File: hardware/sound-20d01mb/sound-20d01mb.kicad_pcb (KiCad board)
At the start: 2 copper layers, 0 parts

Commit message: Updated PCB
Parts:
- added C1: 0.1uF, Capacitor_SMD:C_1206_3216Metric_Pad1.42x1.75mm_HandSolder, F.Cu at (123.2, 76.2)
- added C10: 0.1uF, Capacitor_SMD:C_1206_3216Metric_Pad1.42x1.75mm_HandSolder, F.Cu at (106.7, 48.3)
- added C11: 1uF, Capacitor_SMD:C_1206_3216Metric_Pad1.42x1.75mm_HandSolder, F.Cu at (138.4, 58.4)
- added C12: 0.1uF, Capacitor_SMD:C_1206_3216Metric_Pad1.42x1.75mm_HandSolder, F.Cu at (138.4, 62.2)
- added C13: 0.1uF, Capacitor_SMD:C_1206_3216Metric_Pad1.42x1.75mm_HandSolder, F.Cu at (133.3, 54.6)
- added C14: 0.1uF, Capacitor_SMD:C_1206_3216Metric_Pad1.42x1.75mm_HandSolder, F.Cu at (121.3, 54.0)
- added C15: 4.7uF, Capacitor_SMD:C_1206_3216Metric_Pad1.42x1.75mm_HandSolder, F.Cu at (125.7, 52.1)
- added C16: 0.1uF, Capacitor_SMD:C_1206_3216Metric_Pad1.42x1.75mm_HandSolder, F.Cu at (197.5, 62.2)
- added C17: 10uF, Capacitor_SMD:CP_Elec_4x5.4, F.Cu at (197.5, 52.1)
- added C18: 2.2nF, Capacitor_THT:C_Rect_L7.2mm_W2.5mm_P5.00mm_FKS2_FKP2_MKS2_MKP2, F.Cu at (205.3, 59.1)
- added C19: 2.2uF, Capacitor_SMD:C_1206_3216Metric_Pad1.42x1.75mm_HandSolder, F.Cu at (190.5, 73.0)
- added C2: 0.1uF, Capacitor_SMD:C_1206_3216Metric_Pad1.42x1.75mm_HandSolder, F.Cu at (132.7, 73.0)
- added C20: 2.2uF, Capacitor_SMD:C_1206_3216Metric_Pad1.42x1.75mm_HandSolder, F.Cu at (197.5, 68.6)
- added C21: 10uF, Capacitor_SMD:CP_Elec_4x5.4, F.Cu at (177.8, 67.3)
- added C22: 0.1uF, Capacitor_SMD:C_1206_3216Metric_Pad1.42x1.75mm_HandSolder, F.Cu at (183.5, 67.3)
- added C23: 2.2nF, Capacitor_THT:C_Rect_L7.2mm_W2.5mm_P5.00mm_FKS2_FKP2_MKS2_MKP2, F.Cu at (205.3, 71.8)
- added C24: 10uF, Capacitor_SMD:CP_Elec_4x5.4, F.Cu at (183.5, 78.7)
- added C25: 0.1uF, Capacitor_SMD:C_1206_3216Metric_Pad1.42x1.75mm_HandSolder, F.Cu at (183.5, 73.0)
- added C26: 0.1uF, Capacitor_SMD:C_1206_3216Metric_Pad1.42x1.75mm_HandSolder, F.Cu at (197.5, 73.0)
- added C27: 10uF, Capacitor_SMD:CP_Elec_4x5.4, F.Cu at (197.5, 78.7)
- added C28: 0.1uF, Capacitor_SMD:C_1206_3216Metric_Pad1.42x1.75mm_HandSolder, F.Cu at (229.9, 57.1)
- added C29: 470uF, Capacitor_THT:CP_Radial_D12.5mm_P5.00mm, F.Cu at (226.1, 44.5)
- added C3: 0.1uF, Capacitor_SMD:C_1206_3216Metric_Pad1.42x1.75mm_HandSolder, F.Cu at (117.5, 69.2)
- added C30: 0.1uF, Capacitor_SMD:C_1206_3216Metric_Pad1.42x1.75mm_HandSolder, F.Cu at (236.2, 55.9)
- added C31: 10uF, Capacitor_SMD:C_1210_3225Metric_Pad1.42x2.65mm_HandSolder, F.Cu at (241.3, 38.1)
- added C32: 4700uF, Capacitor_THT:CP_Radial_D18.0mm_P7.50mm, F.Cu at (269.2, 55.9)
- added C33: 2.2uF, Capacitor_SMD:C_1206_3216Metric_Pad1.42x1.75mm_HandSolder, F.Cu at (215.9, 67.3)
- added C34: 0.68uF, Capacitor_THT:C_Rect_L7.2mm_W4.5mm_P5.00mm_FKS2_FKP2_MKS2_MKP2, F.Cu at (256.5, 77.5)
- added C35: 0.22uF, Capacitor_SMD:C_1206_3216Metric_Pad1.42x1.75mm_HandSolder, F.Cu at (238.8, 61.0)
- added C36: 0.22uF, Capacitor_SMD:C_1206_3216Metric_Pad1.42x1.75mm_HandSolder, F.Cu at (238.5, 66.0)
- added C37: 2.2uF, Capacitor_SMD:C_1206_3216Metric_Pad1.42x1.75mm_HandSolder, F.Cu at (215.9, 63.5)
- added C38: 0.68uF, Capacitor_THT:C_Rect_L7.2mm_W4.5mm_P5.00mm_FKS2_FKP2_MKS2_MKP2, F.Cu at (256.5, 55.9)
- added C39: 4700uF, Capacitor_THT:CP_Radial_D18.0mm_P7.50mm, F.Cu at (269.2, 77.5)
- added C4: 0.1uF, Capacitor_SMD:C_1206_3216Metric_Pad1.42x1.75mm_HandSolder, F.Cu at (76.2, 53.3)
- added C40: 2.2uF, Capacitor_SMD:C_1206_3216Metric_Pad1.42x1.75mm_HandSolder, F.Cu at (222.2, 62.2)
- added C41: 1uF, Capacitor_SMD:C_1206_3216Metric_Pad1.42x1.75mm_HandSolder, F.Cu at (222.2, 67.3)
- added C42: 0.1uF, Capacitor_SMD:C_1206_3216Metric_Pad1.42x1.75mm_HandSolder, F.Cu at (229.9, 72.4)
- added C43: 470uF, Capacitor_THT:CP_Radial_D12.5mm_P5.00mm, F.Cu at (226.1, 83.8)
- added C44: 47uF, Capacitor_SMD:CP_Elec_6.3x5.4, F.Cu at (76.2, 71.1)
- added C45: 10uF, Capacitor_SMD:CP_Elec_4x5.4, F.Cu at (49.5, 71.1)
- added C46: 2.2uF, Capacitor_SMD:C_1206_3216Metric_Pad1.42x1.75mm_HandSolder, F.Cu at (49.5, 77.5)
- added C47: 2.2uF, Capacitor_SMD:C_1206_3216Metric_Pad1.42x1.75mm_HandSolder, F.Cu at (67.3, 73.7)
- added C48: 10uF, Capacitor_SMD:CP_Elec_4x5.4, F.Cu at (67.3, 80.0)
- added C49: 10uF, Capacitor_SMD:CP_Elec_4x5.4, F.Cu at (176.5, 132.1)
- added C5: 0.1uF, Capacitor_SMD:C_1206_3216Metric_Pad1.42x1.75mm_HandSolder, F.Cu at (144.8, 62.2)
- added C50: 2.2uF, Capacitor_SMD:C_1206_3216Metric_Pad1.42x1.75mm_HandSolder, F.Cu at (146.1, 121.9)
- added C51: 2.2uF, Capacitor_SMD:C_1206_3216Metric_Pad1.42x1.75mm_HandSolder, F.Cu at (177.8, 113.0)
- added C52: 47uF, Capacitor_SMD:CP_Elec_6.3x5.4, F.Cu at (196.8, 132.1)
- added C53: 0.33uF, Capacitor_SMD:C_1206_3216Metric_Pad1.42x1.75mm_HandSolder, F.Cu at (189.2, 115.6)
- added C54: 0.1uF, Capacitor_SMD:C_1206_3216Metric_Pad1.42x1.75mm_HandSolder, F.Cu at (189.2, 121.9)
- added C55: 10uF, Capacitor_SMD:CP_Elec_4x5.4, F.Cu at (185.4, 132.1)
- added C6: 15pF, Capacitor_SMD:C_1206_3216Metric_Pad1.42x1.75mm_HandSolder, F.Cu at (142.2, 81.3)
- added C7: 15pF, Capacitor_SMD:C_1206_3216Metric_Pad1.42x1.75mm_HandSolder, F.Cu at (135.9, 81.3)
- added C8: 22pF, Capacitor_SMD:C_1206_3216Metric_Pad1.42x1.75mm_HandSolder, F.Cu at (149.2, 74.9)
- added C9: 22pF, Capacitor_SMD:C_1206_3216Metric_Pad1.42x1.75mm_HandSolder, F.Cu at (149.2, 67.3)
- added D1: AMP_LED, LED_SMD:LED_1206_3216Metric_Pad1.42x1.75mm_HandSolder, F.Cu at (152.4, 106.7)
- added D2: MUTE_LED, LED_SMD:LED_1206_3216Metric_Pad1.42x1.75mm_HandSolder, F.Cu at (152.4, 111.8)
- added D3: CRS04, Diode_SMD:D_SOD-123F, F.Cu at (76.2, 63.5)
- added D4: D_PWR_LED, LED_SMD:LED_1206_3216Metric_Pad1.42x1.75mm_HandSolder, F.Cu at (73.7, 86.4)
- added D5: A_PWR_LED, LED_SMD:LED_1206_3216Metric_Pad1.42x1.75mm_HandSolder, F.Cu at (152.4, 121.9)
- added F1: MF-MSMF050-2, Fuse:Fuse_1812_4532Metric_Pad1.30x3.40mm_HandSolder, F.Cu at (76.2, 58.4)
- added H1: MountingHole_Pad, MountingHole:MountingHole_3.2mm_M3_Pad_Via, F.Cu at (38.1, 27.9)
- added H2: MountingHole_Pad, MountingHole:MountingHole_3.2mm_M3_Pad_Via, F.Cu at (270.5, 25.4)
- added H3: MountingHole_Pad, MountingHole:MountingHole_3.2mm_M3_Pad_Via, F.Cu at (35.6, 118.1)
- added H4: MountingHole_Pad, MountingHole:MountingHole_3.2mm_M3_Pad_Via, F.Cu at (271.8, 125.7)
- added J1: USB_B, Connector_USB:USB_B_OST_USB-B1HSxx_Horizontal, F.Cu at (68.6, 58.4)
- added J10: Conn_01x02, Connector_JST:JST_VH_B2P-VH_1x02_P3.96mm_Vertical, F.Cu at (224.8, 104.1)
- added J11: Conn_01x03, Connector_PinHeader_2.54mm:PinHeader_1x03_P2.54mm_Vertical, F.Cu at (166.4, 39.4)
- added J12: Conn_01x04, Connector_PinHeader_2.54mm:PinHeader_1x04_P2.54mm_Vertical, F.Cu at (189.2, 47.0)
- added J13: Conn_01x06, Connector_PinHeader_2.54mm:PinHeader_1x06_P2.54mm_Vertical, F.Cu at (151.1, 39.4)
- added J14: Conn_01x03, Connector_PinHeader_2.54mm:PinHeader_1x03_P2.54mm_Vertical, F.Cu at (208.3, 67.9)
- added J2: Conn_01x04, sound-20d01mb:X977B04, F.Cu at (250.2, 105.4)
- added J3: Conn_02x08_Odd_Even, Connector_PinHeader_2.54mm:PinHeader_2x08_P2.54mm_Vertical, F.Cu at (94.0, 72.4)
- added J4: Conn_02x04_Odd_Even, Connector_PinHeader_2.54mm:PinHeader_2x04_P2.54mm_Vertical, F.Cu at (212.1, 100.3)
- added J5: Conn_01x06, Connector_PinHeader_2.54mm:PinHeader_1x06_P2.54mm_Vertical, F.Cu at (109.2, 68.6)
- added J6: Conn_02x10_Odd_Even, Connector_PinHeader_2.54mm:PinHeader_2x10_P2.54mm_Vertical, F.Cu at (138.4, 41.9)
- added J7: Conn_02x10_Odd_Even, Connector_PinHeader_2.54mm:PinHeader_2x10_P2.54mm_Vertical, F.Cu at (138.4, 87.6)
- added J8: Conn_01x02, Connector_JST:JST_XH_B02B-XH-A_1x02_P2.50mm_Vertical, F.Cu at (49.5, 94.0)
- added J9: Conn_01x02, Connector_JST:JST_XH_B02B-XH-A_1x02_P2.50mm_Vertical, F.Cu at (61.0, 94.0)
- added JP1: Jumper_NC_Dual, Connector_PinHeader_2.54mm:PinHeader_1x03_P2.54mm_Vertical, F.Cu at (96.5, 58.4)
- added JP2: Jumper_3_Bridged12, Connector_PinHeader_2.54mm:PinHeader_1x03_P2.54mm_Vertical, F.Cu at (128.3, 76.2)
- added L1: 22uH, Inductor_SMD:L_Bourns_SRR1260, F.Cu at (246.4, 50.8)
- added L2: 22uH, Inductor_SMD:L_Bourns_SRR1260, F.Cu at (246.4, 77.5)
- added NT1: Net-Tie_2, NetTie:NetTie-2_SMD_Pad2.0mm, F.Cu at (190.5, 76.2)
- added R1: 10K, Resistor_SMD:R_1206_3216Metric_Pad1.42x1.75mm_HandSolder, F.Cu at (104.1, 73.7)
- added R10: 10K, Resistor_SMD:R_1206_3216Metric_Pad1.42x1.75mm_HandSolder, F.Cu at (197.5, 57.8)
- added R11: 22R, Resistor_SMD:R_1206_3216Metric_Pad1.42x1.75mm_HandSolder, F.Cu at (180.3, 53.3)
- added R12: 22R, Resistor_SMD:R_1206_3216Metric_Pad1.42x1.75mm_HandSolder, F.Cu at (180.3, 57.1)
- added R13: 470R, Resistor_SMD:R_1206_3216Metric_Pad1.42x1.75mm_HandSolder, F.Cu at (203.8, 67.3)
- added R14: 22R, Resistor_SMD:R_1206_3216Metric_Pad1.42x1.75mm_HandSolder, F.Cu at (180.3, 61.0)
- added R15: 4.7K, Resistor_SMD:R_1206_3216Metric_Pad1.42x1.75mm_HandSolder, F.Cu at (260.4, 62.2)
- added R16: 4.7K, Resistor_SMD:R_1206_3216Metric_Pad1.42x1.75mm_HandSolder, F.Cu at (260.4, 69.8)
- added R17: 10K, Resistor_SMD:R_1206_3216Metric_Pad1.42x1.75mm_HandSolder, F.Cu at (237.5, 91.4)
- added R18: 10K, Resistor_SMD:R_1206_3216Metric_Pad1.42x1.75mm_HandSolder, F.Cu at (237.5, 96.5)
- added R19: 1K, Resistor_SMD:R_1206_3216Metric_Pad1.42x1.75mm_HandSolder, F.Cu at (181.6, 94.0)
- added R2: 4.7K, Resistor_SMD:R_1206_3216Metric_Pad1.42x1.75mm_HandSolder, F.Cu at (160.0, 39.4)
- added R20: 1K, Resistor_SMD:R_1206_3216Metric_Pad1.42x1.75mm_HandSolder, F.Cu at (181.6, 102.9)
- added R21: 1K, Resistor_SMD:R_1206_3216Metric_Pad1.42x1.75mm_HandSolder, F.Cu at (158.8, 106.7)
- added R22: 10K, Resistor_SMD:R_1206_3216Metric_Pad1.42x1.75mm_HandSolder, F.Cu at (215.9, 55.9)
- added R23: 1K, Resistor_SMD:R_1206_3216Metric_Pad1.42x1.75mm_HandSolder, F.Cu at (158.8, 111.8)
- added R24: 10K, Resistor_SMD:R_1206_3216Metric_Pad1.42x1.75mm_HandSolder, F.Cu at (222.2, 55.9)
- added R25: 330R, Resistor_SMD:R_1206_3216Metric_Pad1.42x1.75mm_HandSolder, F.Cu at (67.3, 86.4)
- added R26: 1K, Resistor_SMD:R_1206_3216Metric_Pad1.42x1.75mm_HandSolder, F.Cu at (158.8, 121.9)
- added R3: 4.7K, Resistor_SMD:R_1206_3216Metric_Pad1.42x1.75mm_HandSolder, F.Cu at (160.0, 44.5)
- added R4: 22R, Resistor_SMD:R_1206_3216Metric_Pad1.42x1.75mm_HandSolder, F.Cu at (82.5, 46.4)
- added R5: 22R, Resistor_SMD:R_1206_3216Metric_Pad1.42x1.75mm_HandSolder, F.Cu at (82.5, 50.2)
- added R6: 390R, Resistor_SMD:R_1206_3216Metric_Pad1.42x1.75mm_HandSolder, F.Cu at (138.4, 66.0)
- added R7: 51R, Resistor_SMD:R_1206_3216Metric_Pad1.42x1.75mm_HandSolder, F.Cu at (114.3, 53.3)
- added R8: 22R, Resistor_SMD:R_1206_3216Metric_Pad1.42x1.75mm_HandSolder, F.Cu at (180.3, 49.5)
- added R9: 470R, Resistor_SMD:R_1206_3216Metric_Pad1.42x1.75mm_HandSolder, F.Cu at (203.8, 63.5)
- added SW1: SW_DIP_x02, Button_Switch_THT:SW_DIP_SPSTx02_Slide_9.78x7.26mm_W7.62mm_P2.54mm, F.Cu at (242.6, 88.9)
- added U1: USBLC6-2SC6, Package_TO_SOT_SMD:SOT-23-6, F.Cu at (76.2, 48.3)
- added U2: STM32F446RCTx, Package_QFP:LQFP-64_10x10mm_P0.5mm, F.Cu at (127.0, 63.5)
- added U3: PCM5142, Package_SO:TSSOP-28_4.4x9.7mm_P0.65mm, F.Cu at (190.5, 64.8)
- added U4: TPA3123D2, Package_SO:HTSSOP-24-1EP_4.4x7.8mm_P0.65mm_EP3.4x7.8mm_Mask2.4x4.68mm_ThermalVias, F.Cu at (229.9, 64.8)
- added U5: PC817, Package_DIP:DIP-4_W7.62mm, F.Cu at (186.7, 94.0)
- added U6: PC817, Package_DIP:DIP-4_W7.62mm, F.Cu at (186.7, 102.9)
- added U7: ADP3338AKCZ-3.3RL7, Package_TO_SOT_SMD:SOT-223-3_TabPin2, F.Cu at (59.7, 73.7)
- added U8: ADP3338AKCZ-3.3RL7, Package_TO_SOT_SMD:SOT-223-3_TabPin2, F.Cu at (180.3, 120.7)
- added U9: L7805ABD2T-TR, Package_TO_SOT_SMD:TO-263-2, F.Cu at (200.7, 119.4)
- added X1: SM7745HEV-12.288M, Oscillator:Oscillator_SMD_Fordahl_DFAS2-4Pin_7.3x5.1mm_HandSoldering, F.Cu at (106.7, 55.9)
- added Y1: 32.768kHz, Crystal:Crystal_SMD_3215-2Pin_3.2x1.5mm, F.Cu at (138.4, 76.2)
- added Y2: 8MHz, Crystal:Crystal_SMD_HC49-SD, F.Cu at (144.8, 71.1)
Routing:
- net +3V3: track 0.00 -> 66.7 mm, vias 0 -> 7
- net +3.3VA: track 0.00 -> 42.6 mm, vias 0 -> 2
- net /Microcontroller Unit/RCC_OSC_IN: track 0.00 -> 23.3 mm
- net DAC_GPIO6: track 0.00 -> 19.2 mm, vias 0 -> 1
- net Net-(R8-Pad2): track 0.00 -> 18.1 mm
- net I2C1_SDA: track 0.00 -> 17.5 mm
- net I2C1_SCL: track 0.00 -> 17.4 mm
- net VBUS: track 0.00 -> 17.4 mm
- net /Microcontroller Unit/USB_D+: track 0.00 -> 16.0 mm
- net DAC_GPIO3: track 0.00 -> 15.9 mm, vias 0 -> 1
- net Net-(R11-Pad2): track 0.00 -> 15.3 mm
- net /Microcontroller Unit/USB_D-: track 0.00 -> 13.1 mm
- net /Microcontroller Unit/NRST: track 0.00 -> 12.3 mm
- net Net-(R12-Pad2): track 0.00 -> 11.8 mm
- net Net-(C21-Pad1): track 0.00 -> 10.8 mm
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- added copper zone on B.Cu, net GNDA
- added copper zone on F.Cu, net GNDA
- added copper zone on B.Cu, net GNDD
- added copper zone on F.Cu, net GNDD
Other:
- board text added: "3"
- board text added: "4"
- board text added: "5"
- board text added: "6"

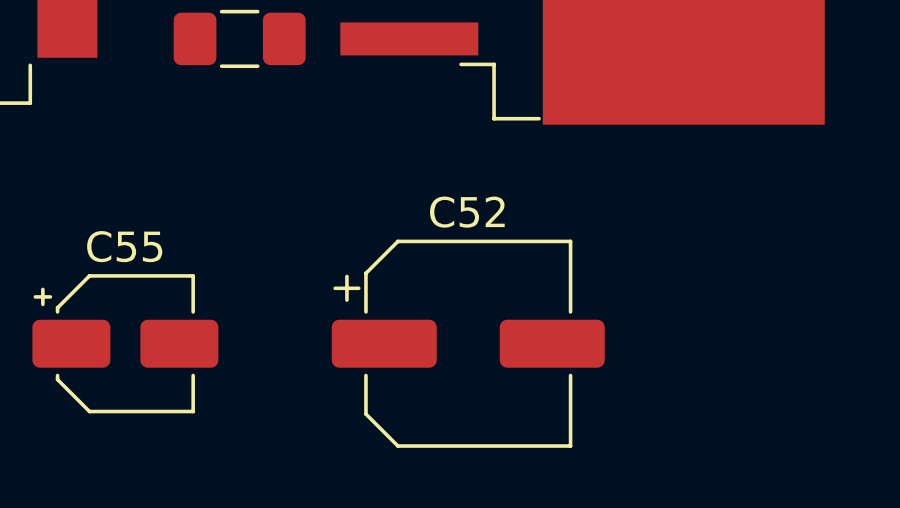
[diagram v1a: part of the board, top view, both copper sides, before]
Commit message: Updated C52 footprint
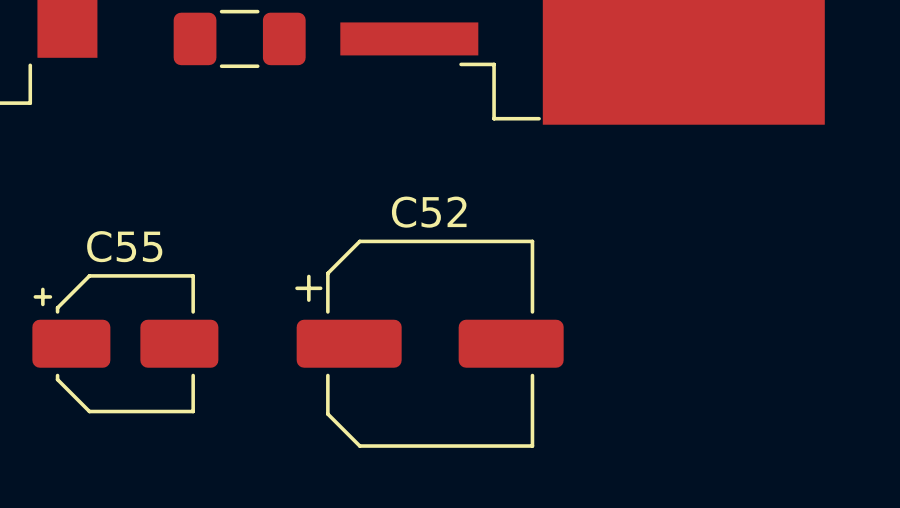
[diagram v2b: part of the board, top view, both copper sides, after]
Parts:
- C52: footprint Capacitor_SMD:CP_Elec_6.3x5.4 -> Capacitor_SMD:CP_Elec_6.3x7.7
- moved C52 1.27 mm to (195.6, 132.1)
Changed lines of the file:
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@@
     )
   )
-  (module Capacitor_SMD:CP_Elec_6.3x5.4 (layer F.Cu)
-    (at 196.85 132.08)
-    (descr "SMD capacitor, aluminum electrolytic, Panasonic C55, 6.3x5.4mm")
-    (tags "capacitor electrolytic")
-    (attr smd)
-    (fp_text reference C52 (at 0 -4.35) (layer F.SilkS)
-      (effects (font (size 1 1) (thickness 0.15)))
-    )
-    (fp_text value 47uF (at 0 4.35) (layer F.Fab)
-      (effects (font (size 1 1) (thickness 0.15)))
-    )
-    (fp_circle (center 0 0) (end 3.15 0) (layer F.Fab) (width 0.1))
-    (fp_line (start 3.3 -3.3) (end 3.3 3.3) (layer F.Fab) (width 0.1))
-    (fp_line (start -2.3 -3.3) (end 3.3 -3.3) (layer F.Fab) (width 0.1))
-    (fp_line (start -2.3 3.3) (end 3.3 3.3) (layer F.Fab) (width 0.1))
-    (fp_line (start -3.3 -2.3) (end -3.3 2.3) (layer F.Fab) (width 0.1))
-    (fp_line (start -3.3 -2.3) (end -2.3 -3.3) (layer F.Fab) (width 0.1))
-    (fp_line (start -3.3 2.3) (end -2.3 3.3) (layer F.Fab) (width 0.1))
-    (fp_line (start -2.704838 -1.33) (end -2.074838 -1.33) (layer F.Fab) (width 0.1))
-    (fp_line (start -2.389838 -1.645) (end -2.389838 -1.015) (layer F.Fab) (width 0.1))
-    (fp_line (start 3.41 3.41) (end 3.41 1.06) (layer F.SilkS) (width 0.12))
-    (fp_line (start 3.41 -3.41) (end 3.41 -1.06) (layer F.SilkS) (width 0.12))
-    (fp_line (start -2.345563 -3.41) (end 3.41 -3.41) (layer F.SilkS) (width 0.12))
-    (fp_line (start -2.345563 3.41) (end 3.41 3.41) (layer F.SilkS) (width 0.12))
-    (fp_line (start -3.41 2.345563) (end -3.41 1.06) (layer F.SilkS) (width 0.12))
-    (fp_line (start -3.41 -2.345563) (end -3.41 -1.06) (layer F.SilkS) (width 0.12))
-    (fp_line (start -3.41 -2.345563) (end -2.345563 -3.41) (layer F.SilkS) (width 0.12))
-    (fp_line (start -3.41 2.345563) (end -2.345563 3.41) (layer F.SilkS) (width 0.12))
-    (fp_line (start -4.4375 -1.8475) (end -3.65 -1.8475) (layer F.SilkS) (width 0.12))
-    (fp_line (start -4.04375 -2.24125) (end -4.04375 -1.45375) (layer F.SilkS) (width 0.12))
-    (fp_line (start 3.55 -3.55) (end 3.55 -1.05) (layer F.CrtYd) (width 0.05))
-    (fp_line (start 3.55 -1.05) (end 4.8 -1.05) (layer F.CrtYd) (width 0.05))
-    (fp_line (start 4.8 -1.05) (end 4.8 1.05) (layer F.CrtYd) (width 0.05))
-    (fp_line (start 4.8 1.05) (end 3.55 1.05) (layer F.CrtYd) (width 0.05))
-    (fp_line (start 3.55 1.05) (end 3.55 3.55) (layer F.CrtYd) (width 0.05))
-    (fp_line (start -2.4 3.55) (end 3.55 3.55) (layer F.CrtYd) (width 0.05))
-    (fp_line (start -2.4 -3.55) (end 3.55 -3.55) (layer F.CrtYd) (width 0.05))
-    (fp_line (start -3.55 2.4) (end -2.4 3.55) (layer F.CrtYd) (width 0.05))
-    (fp_line (start -3.55 -2.4) (end -2.4 -3.55) (layer F.CrtYd) (width 0.05))
-    (fp_line (start -3.55 -2.4) (end -3.55 -1.05) (layer F.CrtYd) (width 0.05))
-    (fp_line (start -3.55 1.05) (end -3.55 2.4) (layer F.CrtYd) (width 0.05))
-    (fp_line (start -3.55 -1.05) (end -4.8 -1.05) (layer F.CrtYd) (width 0.05))
-    (fp_line (start -4.8 -1.05) (end -4.8 1.05) (layer F.CrtYd) (width 0.05))
-    (fp_line (start -4.8 1.05) (end -3.55 1.05) (layer F.CrtYd) (width 0.05))
-    (fp_text user %R (at 0 0) (layer F.Fab)
-      (effects (font (size 1 1) (thickness 0.15)))
-    )
-    (pad 1 smd roundrect (at -2.8 0) (size 3.5 1.6) (layers F.Cu F.Paste F.Mask) (roundrect_rratio 0.15625)
-      (net 18 VCC))
-    (pad 2 smd roundrect (at 2.8 0) (size 3.5 1.6) (layers F.Cu F.Paste F.Mask) (roundrect_rratio 0.15625)
-      (net 11 GNDA))
-    (model ${KISYS3DMOD}/Capacitor_SMD.3dshapes/CP_Elec_6.3x5.4.wrl
-      (at (xyz 0 0 0))
-      (scale (xyz 1 1 1))
-      (rotate (xyz 0 0 0))
-    )
-  )
   (module Capacitor_SMD:C_1206_3216Metric_Pad1.42x1.75mm_HandSolder (layer F.Cu)
     (at 189.23 115.57)
@@
       (at (xyz 0 0 0))
       (scale (xyz 1 1 1))
+      (rotate (xyz 0 0 0))
+    )
+  )
+  (module Capacitor_SMD:CP_Elec_6.3x7.7 (layer F.Cu)
+    (at 195.58 132.08)
+    (descr "SMD capacitor, aluminum electrolytic, Nichicon, 6.3x7.7mm")
+    (tags "capacitor electrolytic")
+    (attr smd)
+    (fp_text reference C52 (at 0 -4.35) (layer F.SilkS)
+      (effects (font (size 1 1) (thickness 0.15)))
+    )
+    (fp_text value 47uF (at 0 4.35) (layer F.Fab)
+      (effects (font (size 1 1) (thickness 0.15)))
+    )
+    (fp_circle (center 0 0) (end 3.15 0) (layer F.Fab) (width 0.1))
+    (fp_line (start 3.3 -3.3) (end 3.3 3.3) (layer F.Fab) (width 0.1))
+    (fp_line (start -2.3 -3.3) (end 3.3 -3.3) (layer F.Fab) (width 0.1))
+    (fp_line (start -2.3 3.3) (end 3.3 3.3) (layer F.Fab) (width 0.1))
+    (fp_line (start -3.3 -2.3) (end -3.3 2.3) (layer F.Fab) (width 0.1))
+    (fp_line (start -3.3 -2.3) (end -2.3 -3.3) (layer F.Fab) (width 0.1))
+    (fp_line (start -3.3 2.3) (end -2.3 3.3) (layer F.Fab) (width 0.1))
+    (fp_line (start -2.704838 -1.33) (end -2.074838 -1.33) (layer F.Fab) (width 0.1))
+    (fp_line (start -2.389838 -1.645) (end -2.389838 -1.015) (layer F.Fab) (width 0.1))
+    (fp_line (start 3.41 3.41) (end 3.41 1.06) (layer F.SilkS) (width 0.12))
+    (fp_line (start 3.41 -3.41) (end 3.41 -1.06) (layer F.SilkS) (width 0.12))
+    (fp_line (start -2.345563 -3.41) (end 3.41 -3.41) (layer F.SilkS) (width 0.12))
+    (fp_line (start -2.345563 3.41) (end 3.41 3.41) (layer F.SilkS) (width 0.12))
+    (fp_line (start -3.41 2.345563) (end -3.41 1.06) (layer F.SilkS) (width 0.12))
+    (fp_line (start -3.41 -2.345563) (end -3.41 -1.06) (layer F.SilkS) (width 0.12))
+    (fp_line (start -3.41 -2.345563) (end -2.345563 -3.41) (layer F.SilkS) (width 0.12))
+    (fp_line (start -3.41 2.345563) (end -2.345563 3.41) (layer F.SilkS) (width 0.12))
+    (fp_line (start -4.4375 -1.8475) (end -3.65 -1.8475) (layer F.SilkS) (width 0.12))
+    (fp_line (start -4.04375 -2.24125) (end -4.04375 -1.45375) (layer F.SilkS) (width 0.12))
+    (fp_line (start 3.55 -3.55) (end 3.55 -1.05) (layer F.CrtYd) (width 0.05))
+    (fp_line (start 3.55 -1.05) (end 4.7 -1.05) (layer F.CrtYd) (width 0.05))
+    (fp_line (start 4.7 -1.05) (end 4.7 1.05) (layer F.CrtYd) (width 0.05))
+    (fp_line (start 4.7 1.05) (end 3.55 1.05) (layer F.CrtYd) (width 0.05))
+    (fp_line (start 3.55 1.05) (end 3.55 3.55) (layer F.CrtYd) (width 0.05))
+    (fp_line (start -2.4 3.55) (end 3.55 3.55) (layer F.CrtYd) (width 0.05))
+    (fp_line (start -2.4 -3.55) (end 3.55 -3.55) (layer F.CrtYd) (width 0.05))
+    (fp_line (start -3.55 2.4) (end -2.4 3.55) (layer F.CrtYd) (width 0.05))
+    (fp_line (start -3.55 -2.4) (end -2.4 -3.55) (layer F.CrtYd) (width 0.05))
+    (fp_line (start -3.55 -2.4) (end -3.55 -1.05) (layer F.CrtYd) (width 0.05))
+    (fp_line (start -3.55 1.05) (end -3.55 2.4) (layer F.CrtYd) (width 0.05))
+    (fp_line (start -3.55 -1.05) (end -4.7 -1.05) (layer F.CrtYd) (width 0.05))
+    (fp_line (start -4.7 -1.05) (end -4.7 1.05) (layer F.CrtYd) (width 0.05))
+    (fp_line (start -4.7 1.05) (end -3.55 1.05) (layer F.CrtYd) (width 0.05))
+    (fp_text user %R (at 0 0) (layer F.Fab)
+      (effects (font (size 1 1) (thickness 0.15)))
+    )
+    (pad 1 smd roundrect (at -2.7 0) (size 3.5 1.6) (layers F.Cu F.Paste F.Mask) (roundrect_rratio 0.15625)
+      (net 18 VCC))
+    (pad 2 smd roundrect (at 2.7 0) (size 3.5 1.6) (layers F.Cu F.Paste F.Mask) (roundrect_rratio 0.15625)
+      (net 11 GNDA))
+    (model ${KISYS3DMOD}/Capacitor_SMD.3dshapes/CP_Elec_6.3x7.7.wrl
+      (at (xyz 0 0 0))
+      (scale (xyz 1 1 1))

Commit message: Updated PCB
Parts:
- moved H4 84.0 mm to (193.0, 96.5)
- moved H2 78.0 mm to (193.0, 34.3)
- moved D1 73.8 mm to (186.7, 41.3), turned to 180 degrees
- moved D2 71.6 mm to (186.7, 48.9), turned to 180 degrees
- moved R21 69.1 mm to (181.0, 41.3)
- moved R23 66.7 mm to (181.0, 48.9)
- moved J8 60.8 mm to (76.2, 39.4)
- moved J9 60.2 mm to (86.4, 39.4)
- moved U6 59.2 mm to (168.9, 46.4)
- moved R20 59.1 mm to (164.5, 46.4)
- moved U5 58.0 mm to (168.9, 38.7)
- moved R19 57.8 mm to (164.5, 38.7)
- moved J3 44.0 mm to (125.7, 102.9)
- moved H3 39.5 mm to (68.6, 96.5)
- moved C5 34.7 mm to (114.3, 78.7)
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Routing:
- net +3.3VA: track 42.6 -> 73.0 mm
- net /Microcontroller Unit/RCC_OSC32_OUT: track 0.00 -> 12.9 mm
- net /Microcontroller Unit/NRST: track 12.3 -> 0.00 mm
- net /Microcontroller Unit/RCC_OSC32_IN: track 0.00 -> 10.2 mm
- net /DAC/DAC_WS: track 0.00 -> 4.64 mm
- net /Microcontroller Unit/RCC_OSC_IN: track 23.3 -> 19.0 mm
- net /DAC/DAC_SD: track 0.00 -> 4.12 mm
- net /DAC/DAC_MCK: track 0.00 -> 4.12 mm
- net /DAC/DAC_CK: track 0.00 -> 3.59 mm
- net Net-(C9-Pad1): track 10.1 -> 13.2 mm
- net ~AMP_SD: track 0.00 -> 2.96 mm
- net Net-(R20-Pad2): track 0.00 -> 2.96 mm
- net Net-(R19-Pad2): track 0.00 -> 2.96 mm
- net AMP_MUTE: track 0.00 -> 2.96 mm
- net Net-(D2-Pad2): track 0.00 -> 2.74 mm
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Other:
- board text added: "GPIO"
- board text added: "MUTE"
- board text added: "ON"

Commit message: Updated PCB
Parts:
- moved J8 51.6 mm to (85.1, 90.2)
- moved J9 51.6 mm to (95.2, 90.2)
- moved D4 50.7 mm to (108.0, 39.4)
- moved R25 50.7 mm to (101.6, 39.4)
- moved C45 46.2 mm to (87.6, 39.4)
- moved C48 42.6 mm to (95.2, 39.4)
- moved C46 41.4 mm to (87.6, 50.8)
- moved J3 37.5 mm to (160.0, 87.6), turned to 270 degrees
- moved U7 32.5 mm to (95.2, 48.3)
- moved C47 28.4 mm to (87.6, 45.7)
- moved F1 20.1 mm to (97.8, 77.5)
- moved U1 18.8 mm to (99.1, 65.4)
- moved C4 18.8 mm to (99.1, 70.5)
- moved R4 18.8 mm to (105.4, 63.5)
- moved R5 18.8 mm to (105.4, 67.3)
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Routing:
- net /Microcontroller Unit/USB_OTG_FS_DM: track 0.00 -> 15.1 mm
- net /Microcontroller Unit/USB_OTG_FS_DP: track 0.00 -> 15.0 mm
- net /Microcontroller Unit/I2S_CKIN: track 0.00 -> 10.9 mm
- net /Microcontroller Unit/USB_D+: track 16.0 -> 6.62 mm
- net /Microcontroller Unit/USB_D-: track 13.1 -> 4.13 mm
- net VBUS: track 17.4 -> 13.1 mm
- net Net-(R7-Pad2): track 0.00 -> 3.98 mm
- net +3V3: track 66.7 -> 70.4 mm
- net GNDD: vias 16 -> 18

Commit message: Updated PCB
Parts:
- moved D5 98.1 mm to (229.2, 61.0), turned to 180 degrees
- moved R26 88.9 mm to (223.5, 61.0)
- moved C45 84.6 mm to (64.1, 120.7), turned to 270 degrees
- moved C48 80.0 mm to (64.1, 113.0), turned to 90 degrees
- moved C46 72.1 mm to (69.8, 120.7), turned to 270 degrees
- moved U7 70.8 mm to (77.5, 116.8)
- moved C47 70.8 mm to (69.8, 114.3), turned to 90 degrees
- moved C31 70.3 mm to (188.0, 83.8)
- moved C52 69.9 mm to (182.2, 63.5), turned to 270 degrees
- moved J10 68.7 mm to (168.9, 64.1)
- moved C38 66.5 mm to (209.6, 103.0), turned to 270 degrees
- moved C40 63.8 mm to (170.2, 99.1), turned to 180 degrees
- moved C41 61.3 mm to (172.7, 103.5), turned to 270 degrees
- moved R24 61.0 mm to (170.2, 87.6), turned to 180 degrees
- moved C29 60.2 mm to (176.5, 78.7)
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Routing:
- net +5VA: track 0.00 -> 124.2 mm, vias 0 -> 3
- net VCC: track 0.00 -> 88.8 mm
- net +5V: track 0.00 -> 73.4 mm
- net PB5: track 0.00 -> 28.0 mm
- net /Microcontroller Unit/SWDIO: track 0.00 -> 25.1 mm
- net PB4: track 0.00 -> 24.0 mm
- net +3.3VA: track 73.0 -> 95.2 mm, vias 2 -> 3
- net /Microcontroller Unit/SWO: track 0.00 -> 21.6 mm
- net PB8: track 0.00 -> 19.6 mm
- net +3V3: track 70.4 -> 89.7 mm, vias 7 -> 9
- net /Microcontroller Unit/SWCLK: track 0.00 -> 14.7 mm
- net ~AMP_SD: track 2.96 -> 16.2 mm
- net /Microcontroller Unit/BOOT0: track 0.00 -> 10.8 mm
- net Net-(D3-Pad2): track 0.00 -> 10.7 mm
- net AMP_MUTE: track 2.96 -> 13.5 mm
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- added copper zone on F.Cu, net +3.3VA
- added copper zone on F.Cu, net +3V3
- added copper zone on B.Cu, net /Amplifier/LOUT
- added copper zone on B.Cu, net /Amplifier/ROUT
- added copper zone on F.Cu, net Net-(C32-Pad1)
- added copper zone on F.Cu, net Net-(C38-Pad2)
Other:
- board outline added: 199.4 x 69.9 mm
- board text added: "+3V3"
- board text added: "GNDD"
- board text added: "NRST"
- board text added: "SWCLK"
- board text added: "SWDIO"
- board text added: "SWO"
- board text added: "Sound-20D01MB Revision: 0"

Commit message: Updated PCB
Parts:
- moved J8 67.6 mm to (123.2, 110.5)
- moved R3 16.3 mm to (125.7, 63.5), turned to 270 degrees
- moved R2 9.16 mm to (120.7, 63.5), turned to 270 degrees
- moved J3 8.89 mm to (133.3, 119.4)
- moved J5 8.54 mm to (90.2, 100.3), turned to 270 degrees
- moved D5 6.98 mm to (236.2, 61.0)
- moved R26 6.98 mm to (230.5, 61.0)
- moved D4 5.72 mm to (67.3, 61.0), turned to 0 degrees
- moved R25 5.72 mm to (73.0, 61.0), turned to 180 degrees
- moved J4 4.02 mm to (226.1, 64.8)
- moved C35 3.81 mm to (188.0, 94.6)
- moved C36 3.81 mm to (188.0, 98.4)
- moved J11 2.54 mm to (121.9, 68.6), turned to 90 degrees
- moved R7 1.49 mm to (90.2, 78.3)
- moved C1 1.29 mm to (123.2, 100.3)
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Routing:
- net /DAC/DAC_WS: track 4.64 -> 52.6 mm
- net /DAC/DAC_SD: track 4.12 -> 51.6 mm, vias 0 -> 1
- net /DAC/DAC_MCK: track 4.12 -> 51.5 mm
- net /DAC/DAC_CK: track 3.59 -> 47.3 mm, vias 0 -> 1
- net GAIN0: track 0.00 -> 38.5 mm, vias 0 -> 1
- net GAIN1: track 0.00 -> 38.2 mm, vias 0 -> 1
- net ~AMP_SD: track 16.2 -> 48.9 mm
- net I2C1_SDA: track 16.3 -> 46.6 mm
- net GNDD: track 1.44 -> 31.3 mm
- net AMP_MUTE: track 13.5 -> 42.4 mm
- net I2C1_SCL: track 15.3 -> 43.1 mm
- net +5V: track 73.4 -> 98.2 mm
- net PA7: track 0.00 -> 22.3 mm
- net PA5: track 0.00 -> 21.6 mm
- net PA6: track 0.00 -> 18.9 mm
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- added copper zone on F.Cu, net Net-(C35-Pad2)
- added copper zone on F.Cu, net Net-(C36-Pad2)
- added copper zone on B.Cu, net VCC
- added copper zone on F.Cu, net VCC
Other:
- board text added: "+"
- board text added: "+5V"
- board text added: "+5VA"
- board text added: "+BATT"
- board text added: "Analog"
- board text added: "CK"
- board text added: "Digital"
- board text added: "GAIN0"
- board text added: "GAIN1"
- board text added: "GNDA"
- board text added: "L+"
- board text added: "L-"
- board text added: "MCK"
- board text added: "Minimum load impedance: 4 Ohms"
- board text added: "PA0"
- board text added: "PA1"
- board text added: "PA10"
- board text added: "PA15"
- board text added: "PA2"
- board text added: "PA3"
- board text added: "PA4"
- board text added: "PA5"
- board text added: "PA6"
- board text added: "PA7"
- board text added: "PA8"
- board text added: "PB0"
- board text added: "PB1"
- board text added: "PB10"
- board text added: "PB13"
- board text added: "PB14"
- board text added: "PB15"
- board text added: "PB2"
- board text added: "PB4"
- board text added: "PB5"
- board text added: "PB8"
- board text added: "PC1"
- board text added: "PC10"
- board text added: "PC11"
- board text added: "PC12"
- board text added: "PC13"
- board text added: "PC3"
- board text added: "PC6"
- board text added: "PC7"
- board text added: "PC8"
- board text added: "PD2"
- board text added: "R+"
- board text added: "R-"
- board text added: "SCL"
- board text added: "SD"
- board text added: "SDA"
- board text added: "WS"
